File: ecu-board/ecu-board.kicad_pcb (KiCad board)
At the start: 2 copper layers, 180 x 130 mm, 63 parts, among them J1 MicroSquirt_connector, J10 Injector connector, J11 Cockpit connector, J12 EGO connector, J13 Chrankshaft Hall connector, J14 Camshaft Hall connector, J15 Ignition 1 connector, J16 Ignition 2 connector, J17 Camera connector, J18 Wheel Hall connector, J19 Speed sensor connector, J2 Battery power conenctor, J20 CAN connector, J21 12V connector, J22 PWRGND connector, J3 MS_breakout_conn, J4 Motor connector, J5 Serial DB9 connector, J6 Controller connector, J7 Backlight connector, J8 IAT connector, J9 CLT connector, K1 Main power relay, K2 Start motor relay, U1 MAP Sensor

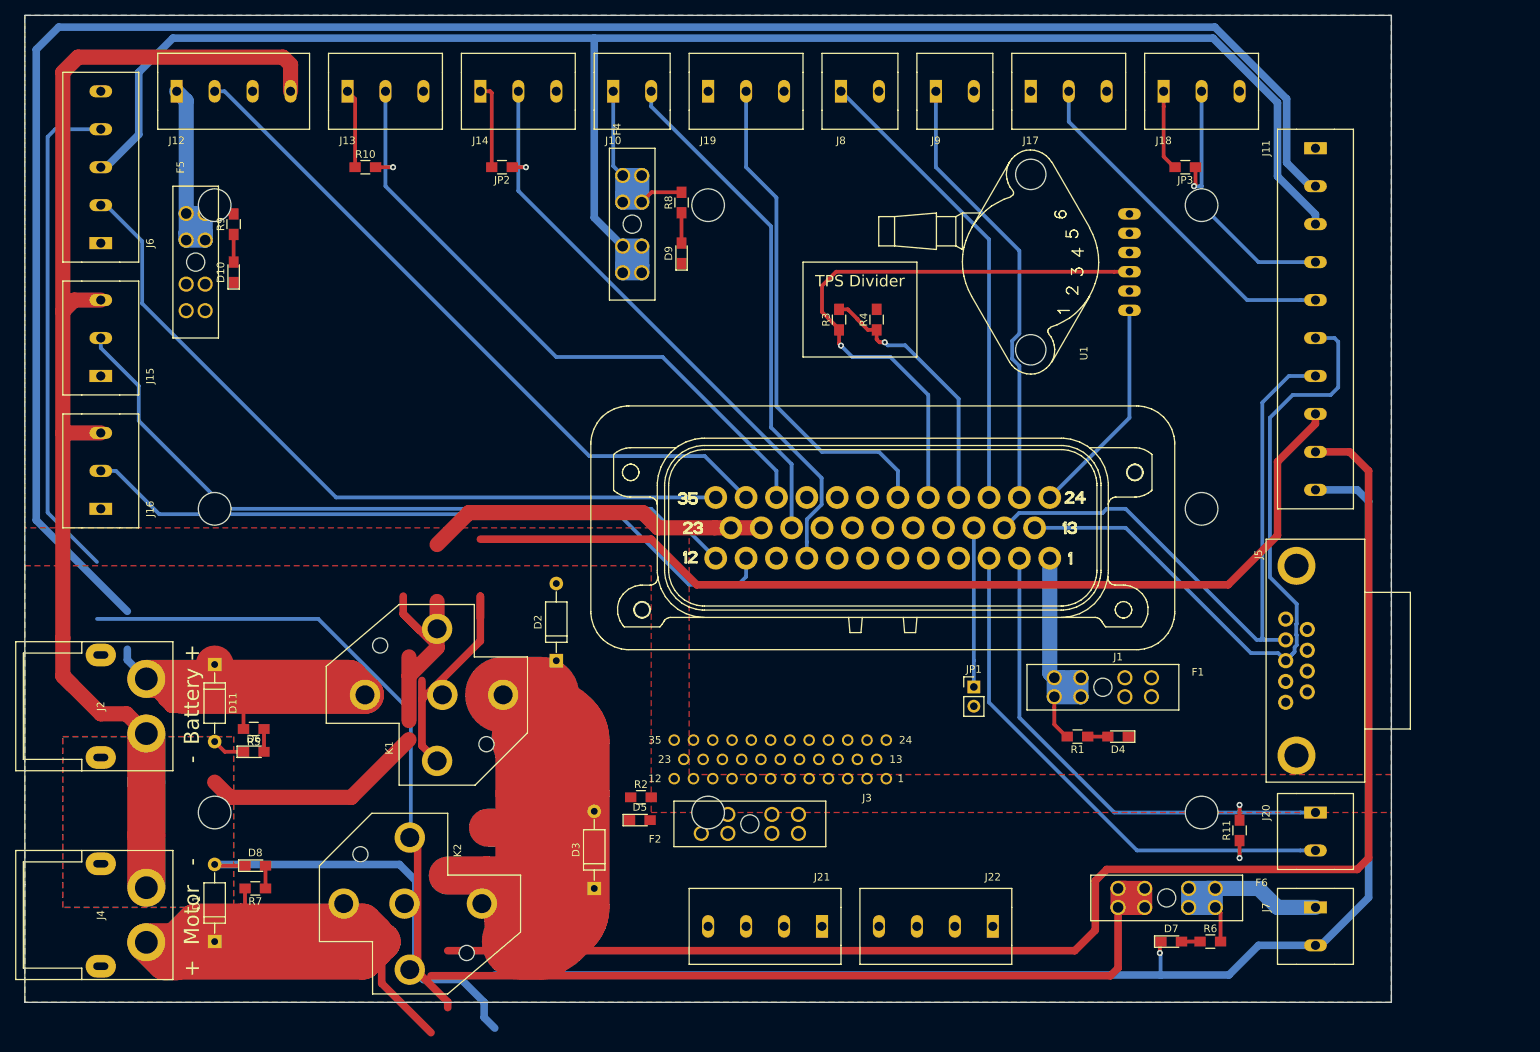
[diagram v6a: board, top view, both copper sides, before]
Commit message: Split MicroSquirt breakout connector into three separate connectors. Old connector was impossible to route.
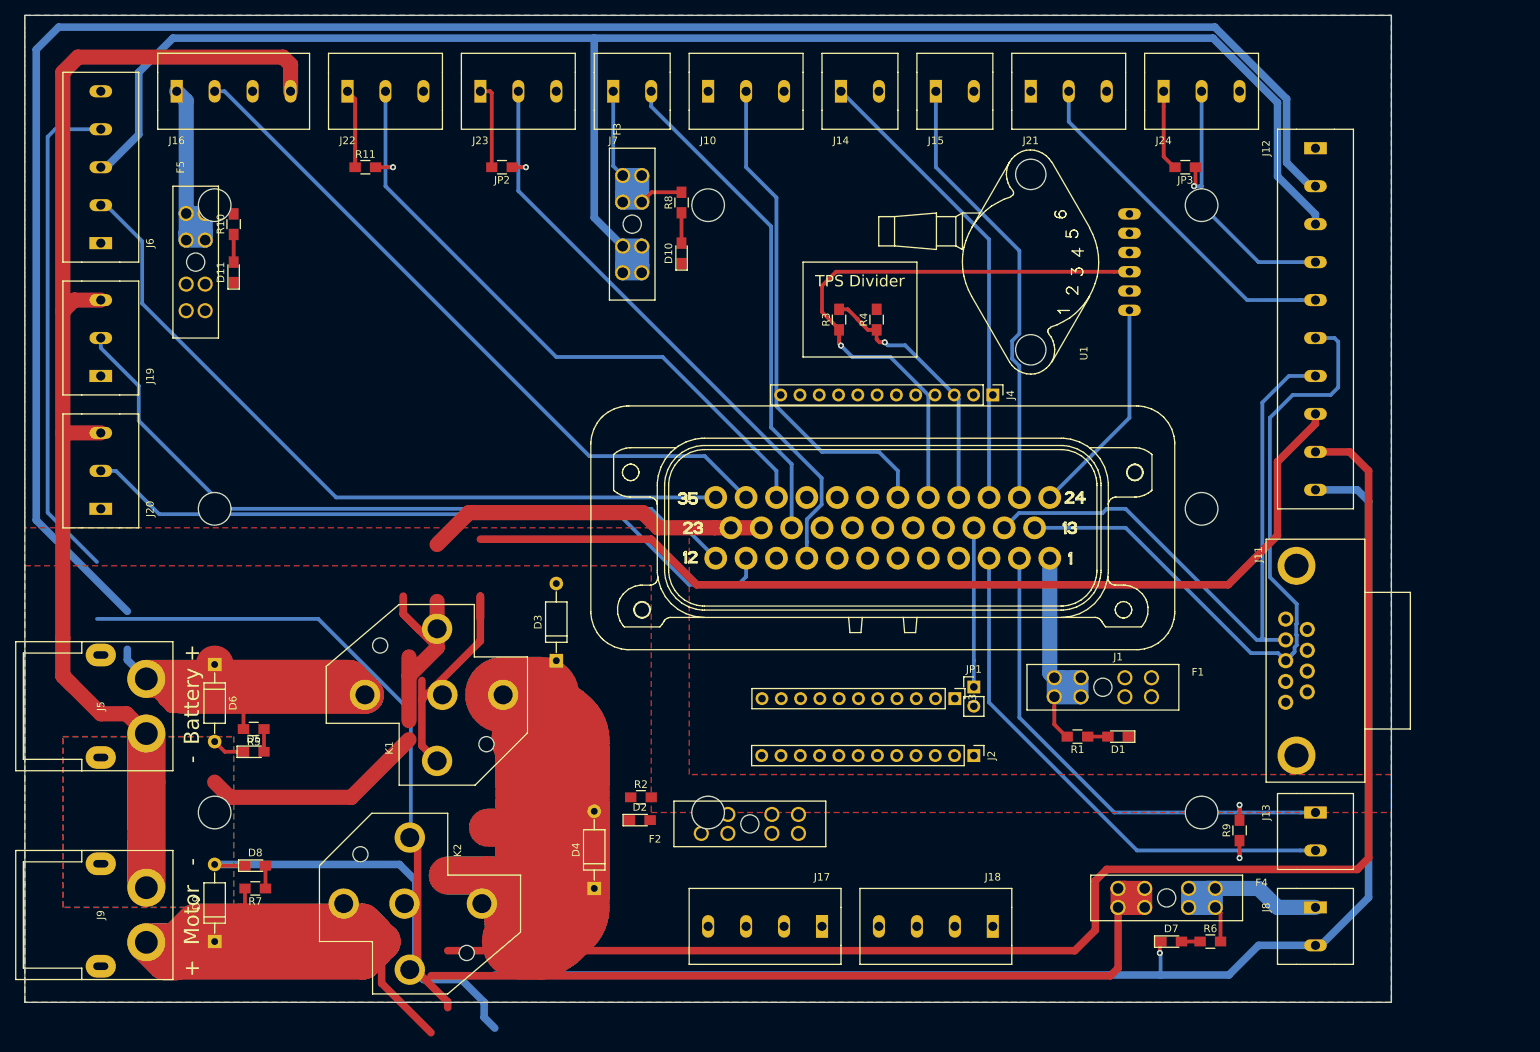
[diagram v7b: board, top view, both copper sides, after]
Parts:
- added J2: MicroSquirt_Breakout, Connector_PinHeader_2.54mm:PinHeader_1x12_P2.54mm_Vertical, F.Cu at (160.0, 132.5)
- added J4: MicroSquirt_Breakout, Connector_PinHeader_2.54mm:PinHeader_1x12_P2.54mm_Vertical, F.Cu at (162.5, 85.0)
- J3: value MS_breakout_conn -> MicroSquirt_Breakout; footprint ecu-board-footprints:MicroSquirt_35Pin -> Connector_PinHeader_2.54mm:PinHeader_1x11_P2.54mm_Vertical
- moved J3 24.4 mm to (157.5, 125.0), turned to 270 degrees
- renumbered D4 to D1, D9 to D10, D10 to D11, D5 to D2, D2 to D3, D3 to D4, D6 to D5, D11 to D6, D1 to D9, F4 to F3, F6 to F4, J19 to J10, J5 to J11, J11 to J12, J20 to J13, J8 to J14, J9 to J15, J12 to J16, J21 to J17, J22 to J18, J15 to J19, J16 to J20, J17 to J21, J13 to J22, J14 to J23, J18 to J24, J2 to J5, J10 to J7, J7 to J8, J4 to J9, R9 to R10, R10 to R11, R11 to R9
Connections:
- J3 pad 1: Net-(F2-Pad1) -> /serial_RX
- J3 pad 10: /injector_2 -> GNDPWR
- J3 pad 11: /ignition_2 -> GNDPWR
- J3 pad 2: /CANH -> /serial_TX
- J3 pad 3: /CANL -> /bootload
- J3 pad 4: /VRIN2+ -> /accel_led
- J3 pad 5: /spare_in2 -> /warm-up
- J3 pad 6: /flex_fuel -> GNDS
- J3 pad 7: /fidle -> GNDS
- J3 pad 8: /fuel_pump -> GNDS
- J3 pad 9: /injector_1 -> /cam_hall_signal

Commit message: Change block terminal article.
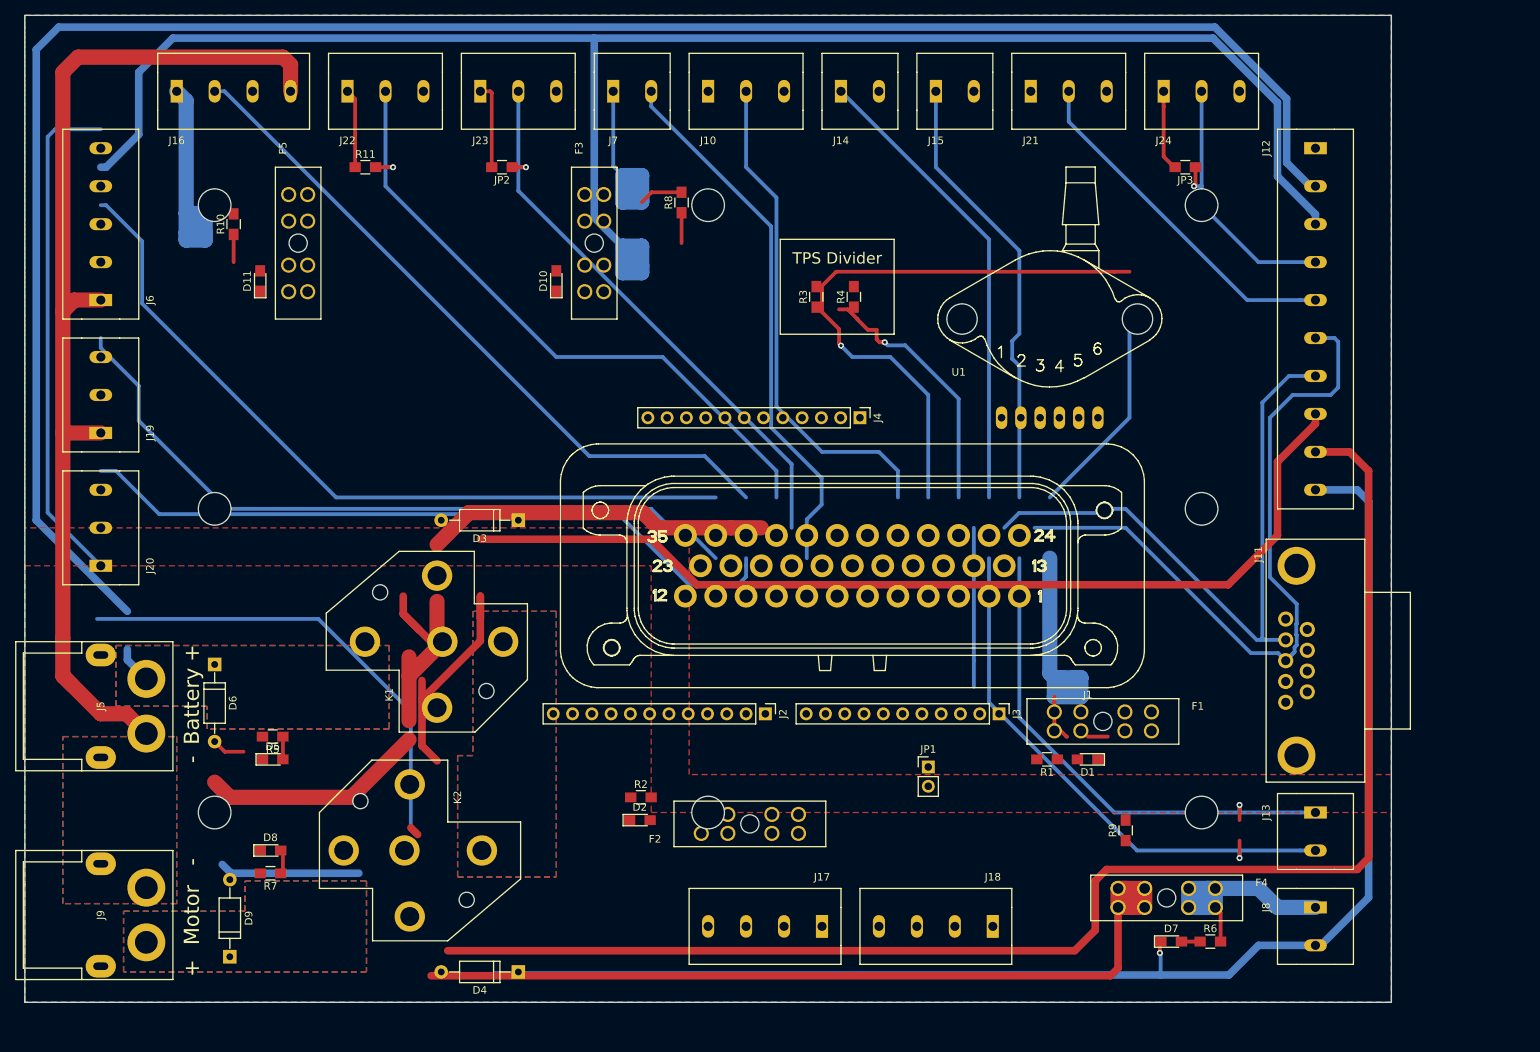
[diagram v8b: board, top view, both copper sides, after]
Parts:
- moved J2 28.0 mm to (132.5, 127.0)
- moved D3 19.2 mm to (100.0, 101.5), turned to 180 degrees
- moved J4 17.8 mm to (145.0, 88.0)
- moved D10 16.9 mm to (105.0, 70.0)
- moved R9 15.0 mm to (180.0, 142.3)
- moved D4 14.9 mm to (100.0, 161.0), turned to 180 degrees
- moved F5 13.7 mm to (71.0, 65.0)
- moved JP1 12.1 mm to (154.0, 134.0)
- moved U1 7.91 mm to (170.0, 75.0), turned to 0 degrees
- moved J19 7.50 mm to (45.0, 90.0)
- moved J20 7.50 mm to (45.0, 107.5)
- moved J6 7.50 mm to (45.0, 72.5)
- moved K1 7.00 mm to (90.0, 117.5)
- moved K2 7.00 mm to (85.0, 145.0)
- moved J1 6.40 mm to (144.0, 107.5)
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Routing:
- net /relay_to_start_motor: track 318.4 -> 120.0 mm
- net +BATT: track 435.8 -> 267.2 mm
- net /button_to_start_motor_relay: track 342.7 -> 189.2 mm
- net GNDPWR: track 533.8 -> 422.1 mm
- net GNDS: track 0.00 -> 34.4 mm, vias 0 -> 1
- net /TPS_input: track 34.4 -> 0.00 mm, vias 1 -> 0
- net Net-(K1-Pad87a): track 0.00 -> 31.4 mm
- net /button_to_main_relay: track 159.4 -> 128.2 mm
- net +12V: track 167.9 -> 192.7 mm
- net /serial_TX: track 85.4 -> 106.4 mm
- net /bootload: track 21.0 -> 0.00 mm
- net Net-(F1-Pad1): track 43.1 -> 45.7 mm
- net Net-(D1-Pad2): track 2.65 -> 0.00 mm
- added copper zone on F.Cu, net +12V
- added copper zone on B.Cu, net +BATT
- added copper zone on F.Cu, net +BATT
- added copper zone on B.Cu, net /relay_to_start_motor
- added copper zone on F.Cu, net /relay_to_start_motor
